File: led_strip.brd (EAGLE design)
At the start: 44.5 x 15.8 mm, 26 parts, among them IC1 REG1117, IC2 MEGA8-AI, U1 MIC9.7MM, X1 USB-SMD-NS, Y1 16MHz

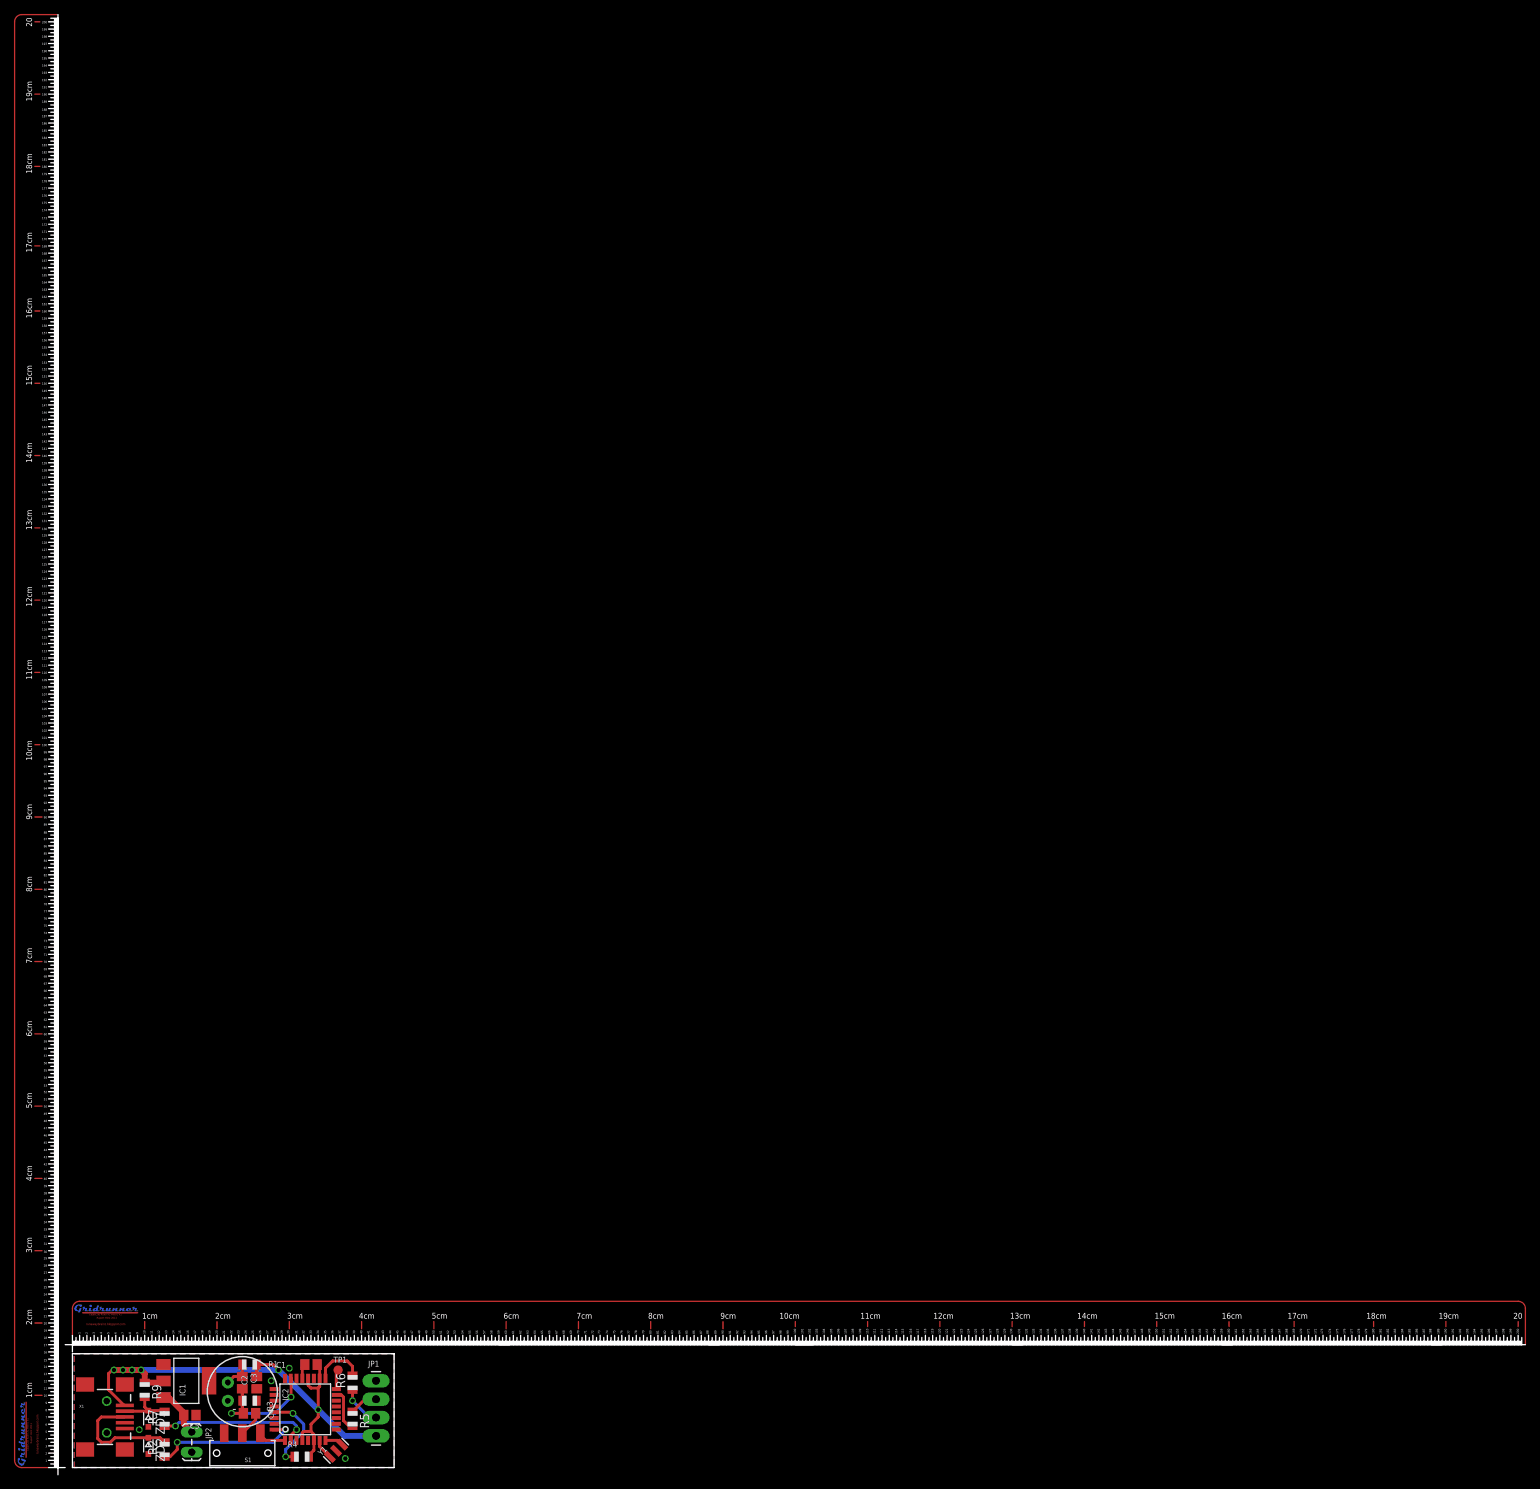
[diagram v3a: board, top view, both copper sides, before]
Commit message: Fixed up layout for ordering.
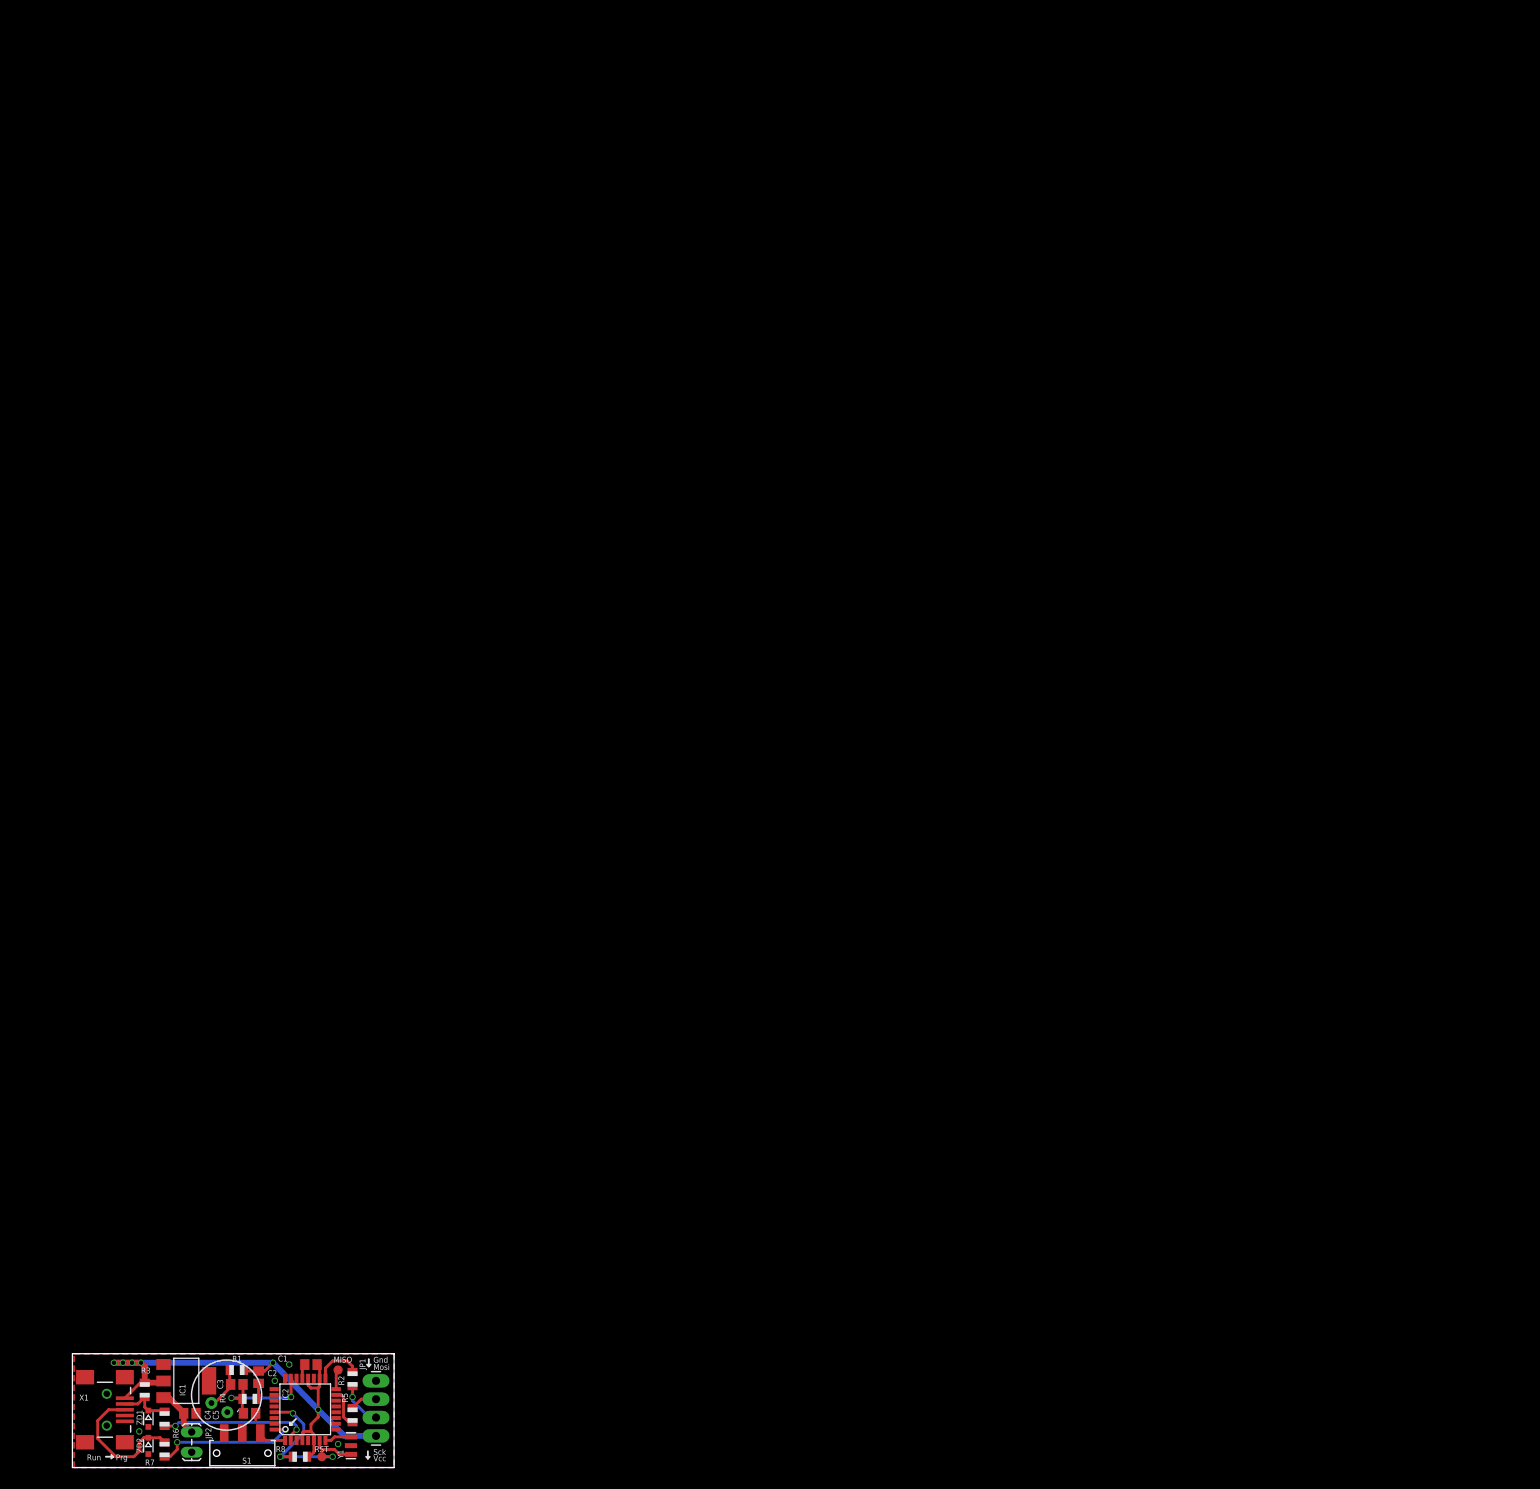
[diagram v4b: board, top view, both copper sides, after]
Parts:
- removed R9: 1.5k, adafruit:R0805
- removed U$1, U$2: (no value), CAD Ruler_EagleCad Gridrunner XL Metric V1 (Rupert Hirst 2011):RULER
- added R8: 10k, adafruit:R0805
- added RST: PTR1B1,27, testpad:B1,27
- C4: value 0.1uf -> 10uf
- C5: value 10uf -> 0.1uf
- R2: value 68 -> 330
- R3: value 10k -> 1.5k
- R6: value 330 -> 68
- moved R2 27.8 mm to (38.8, 12.2)
- moved R6 26.5 mm to (12.8, 6.75)
- moved R3 14.6 mm to (10.0, 10.8), turned to 270 degrees
- moved R4 10.8 mm to (24.5, 9.50)
- moved C5 8.25 mm to (24.5, 7.50)
- moved C4 8.25 mm to (16.2, 7.50)
- moved R7 4.25 mm to (12.8, 2.50)
- moved U1 2.22 mm to (21.3, 10.0), turned to 60 degrees
- moved Y1 2.18 mm to (38.5, 3.03), turned to 90 degrees
- moved R1 1.90 mm to (22.8, 13.5)
- moved X1 1.00 mm to (4.75, 8.00)
- moved C2 0.79 mm to (25.8, 12.5)
- moved C3 0.79 mm to (22.8, 11.5), turned to 0 degrees
- moved R5 0.50 mm to (38.8, 7.25)
- renumbered TP1 to MISO
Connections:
- net GND: now also R4.1; no longer R3.1
- net N$1: now also R2.2; no longer R6.2
- net N$11: now also R6.1; no longer R7.1
- net N$12: now also R7.1; no longer R2.1
- net N$14: now also R2.1; no longer R6.1
- net N$20: now also C4.1; no longer C5.1
- net N$4: now also R7.2; no longer R2.2
- net N$5: now also R3.2, R6.2; no longer R7.2, R9.2
- net N$7: now also R8.2, RST.TP; no longer R4.2
- net N$9: now also C5.1, R4.2; no longer C4.1, R3.2
- net VCC: now also R3.1, R8.1; no longer R4.1, R9.1
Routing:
- net N$7: track 11.5 -> 21.8 mm, vias 2 -> 3
- net N$9: track 20.2 -> 16.9 mm
- net VCC: track 80.3 -> 77.4 mm
- net N$6: track 2.87 -> 5.69 mm
- net N$4: track 16.4 -> 19.2 mm
- net N$10: track 3.99 -> 6.27 mm
- net N$8: track 2.56 -> 3.74 mm
- net N$15: track 5.94 -> 5.44 mm
- net N$14: track 5.72 -> 6.22 mm
- net N$1: track 7.13 -> 6.63 mm
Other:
- board text added: "Gnd"
- board text added: "Jeremy Ruhland"
- board text added: "Mosi"
- board text added: "Prg"
- board text added: "Run"
- board text added: "Sck"
- board text added: "Vcc"
- board text added: "http://github.com/JeremyRuhland/"
- board text added: "led-strip-controller"

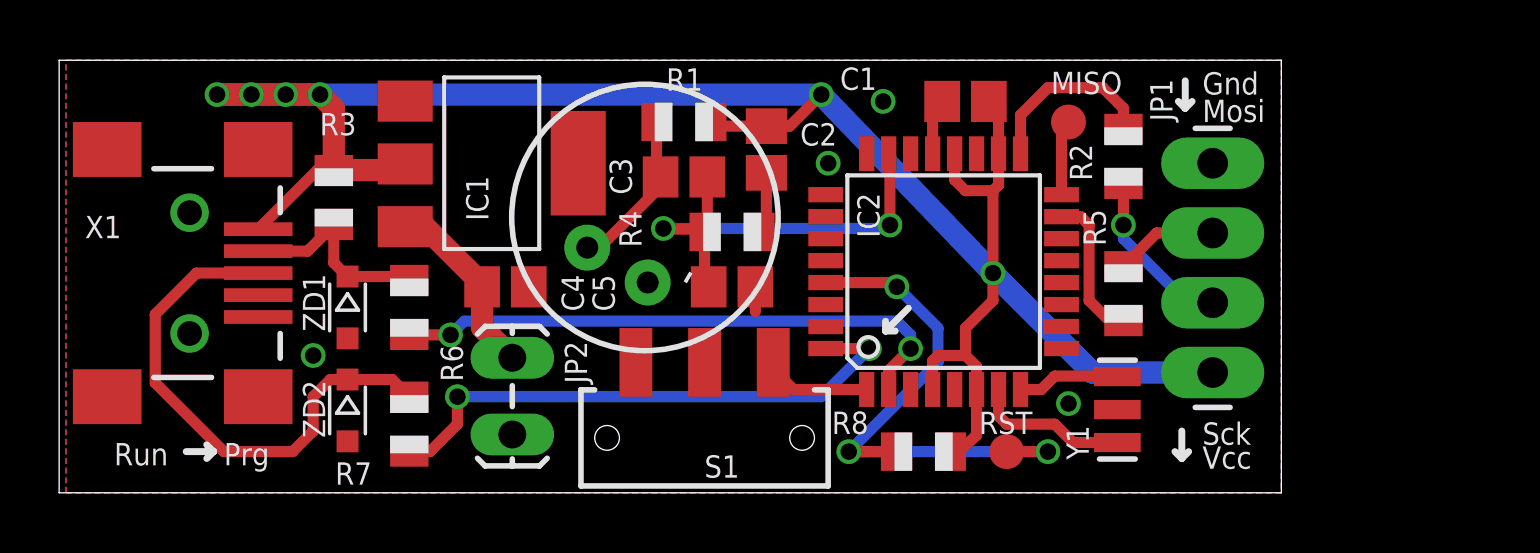
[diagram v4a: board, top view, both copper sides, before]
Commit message: still adding io pins, fixed mic input issue
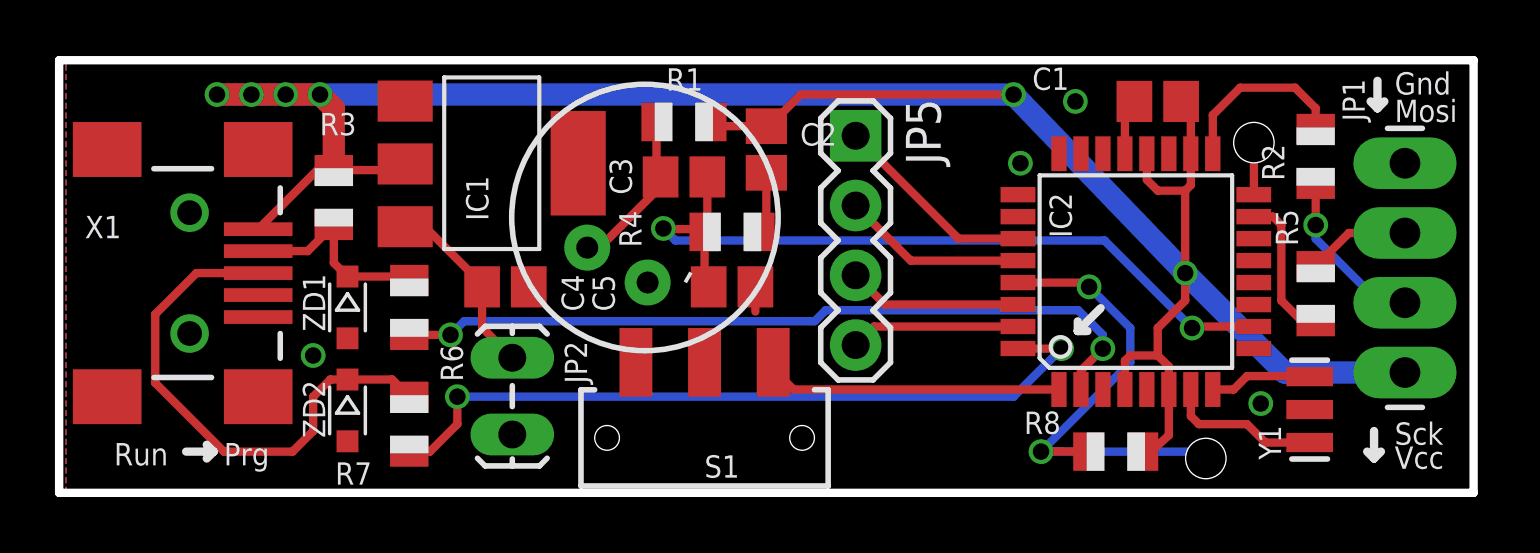
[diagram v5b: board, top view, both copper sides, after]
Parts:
- removed MISO, RST: PTR1B1,27, testpad:B1,27
- added JP3, JP4: M01POGOPIN_HOLE_0.58, sparkfun:1X01_POGOPIN_HOLE_0.58
- added JP5: (no value), sparkfun:1X04
- moved C1 7.00 mm to (40.0, 14.2)
- moved IC2 7.00 mm to (39.2, 8.05)
- moved JP1 7.00 mm to (49.0, 12.0)
- moved R2 7.00 mm to (45.8, 12.2)
- moved R5 7.00 mm to (45.8, 7.25)
- moved R8 7.00 mm to (38.5, 1.50)
- moved Y1 7.00 mm to (45.5, 3.03)
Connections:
- new net N$16: IC2.30, JP5.3
- new net N$17: IC2.31, JP5.4
- new net N$18: IC2.28, JP5.2
- new net N$19: IC2.27, JP5.1
- net N$2: now also JP4.1; no longer MISO.TP
- net N$7: now also JP3.1; no longer RST.TP
- net N$9: now also IC2.10; no longer IC2.23
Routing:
- net VCC: track 77.4 -> 91.4 mm
- net N$9: track 16.9 -> 28.9 mm
- net N$19: track 0.00 -> 7.46 mm
- net N$11: track 21.0 -> 28.3 mm
- net N$13: track 3.96 -> 11.0 mm
- net N$12: track 20.7 -> 27.7 mm
- net N$18: track 0.00 -> 6.74 mm
- net N$16: track 0.00 -> 6.35 mm
- net N$17: track 0.00 -> 6.19 mm
- net N$7: track 21.8 -> 19.2 mm, vias 3 -> 2
- net N$2: track 2.75 -> 1.90 mm
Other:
- board size 44.5 x 15.8 mm -> 51.5 x 15.8 mm
